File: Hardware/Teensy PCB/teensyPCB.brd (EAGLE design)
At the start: 100 x 50 mm, 27 parts, among them U2 USD-SOCKETNEW

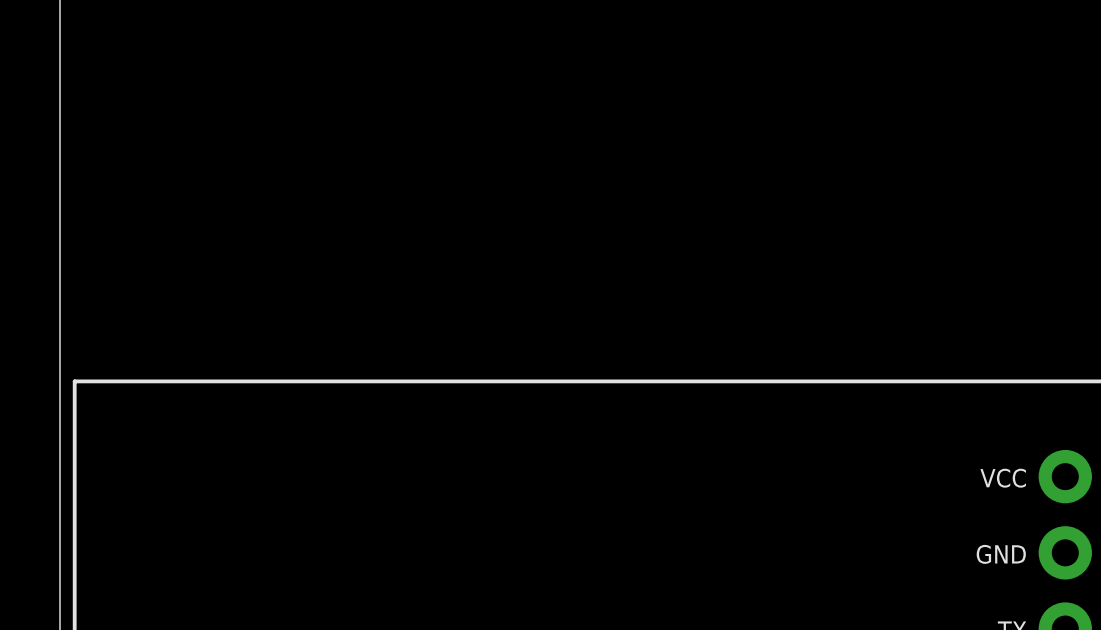
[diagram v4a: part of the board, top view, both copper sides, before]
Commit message: Added "state" push buttons
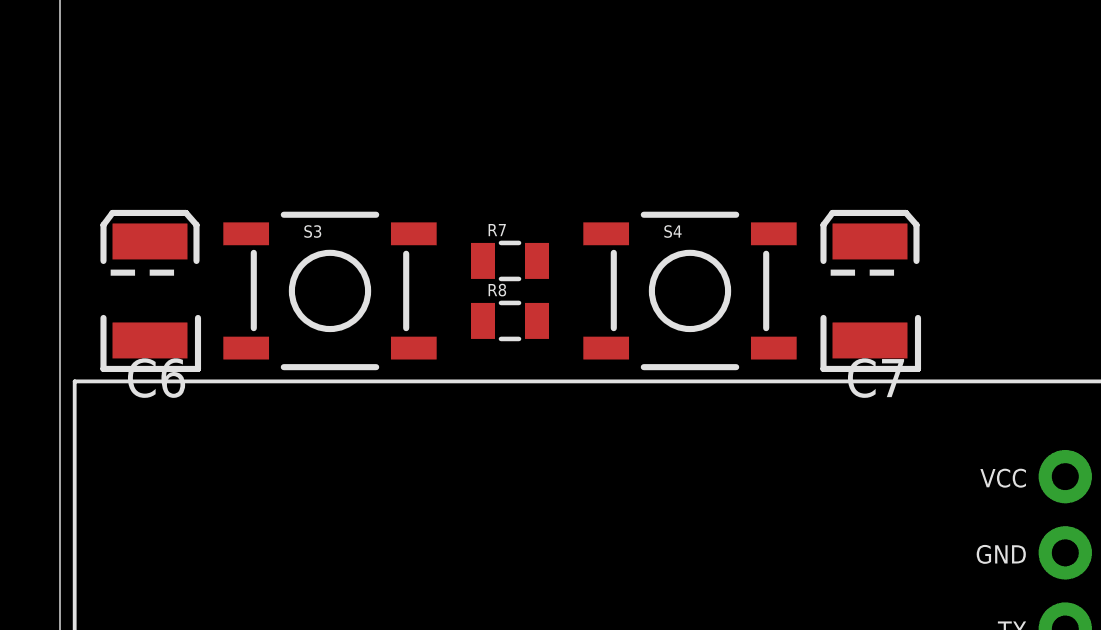
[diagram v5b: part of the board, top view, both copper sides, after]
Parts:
- added C6, C7: 100nF, SparkFun-Capacitors:EIA3528
- added R7, R8: 10k, SparkFun-Resistors:0805
- added S3, S4: TAC_SWITCHSMD, SparkFun-Retired:TACTILE-SWITCH-SMD
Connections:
- new net N$10: C7.C, R8.2, S4.3, S4.4, U$1.27
- new net N$4: C6.C, R7.2, S3.3, S3.4, U$1.28
- net 5V: now also C6.A, C7.A, S3.1, S3.2, S4.1, S4.2
- net GND: now also R7.1, R8.1
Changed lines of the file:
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@@
 <?xml version="1.0" encoding="utf-8"?>
 <!DOCTYPE eagle SYSTEM "eagle.dtd">
-<eagle version="7.5.0">
+<eagle version="7.2.0">
 <drawing>
 <settings>
@@
 <element name="C5" library="SparkFun-Capacitors" package="EIA3528" value="10uF" x="74" y="11"/>
 <element name="BAT1" library="SparkFun-Electromechanical" package="BATTCOM_20MM_PTH" value="" x="87" y="33" rot="R180"/>
+<element name="S3" library="SparkFun-Retired" package="TACTILE-SWITCH-SMD" value="TAC_SWITCHSMD" x="9" y="18">
+<attribute name="PROD_ID" value="SWCH-08247" x="9" y="32" size="1.778" layer="27" display="off"/>
+</element>
+<element name="R7" library="SparkFun-Resistors" package="0805" value="10k" x="15" y="19"/>
+<element name="C6" library="SparkFun-Capacitors" package="EIA3528" value="100nF" x="3" y="18" rot="R90"/>
+<element name="S4" library="SparkFun-Retired" package="TACTILE-SWITCH-SMD" value="TAC_SWITCHSMD" x="21" y="18">
+<attribute name="PROD_ID" value="SWCH-08247" x="9" y="32" size="1.778" layer="27" display="off"/>
+</element>
+<element name="R8" library="SparkFun-Resistors" package="0805" value="10k" x="15" y="17"/>
+<element name="C7" library="SparkFun-Capacitors" package="EIA3528" value="100nF" x="27" y="18" rot="R90"/>
 </elements>
 <signals>
@@
 <contactref element="R6" pad="1"/>
 <contactref element="BAT1" pad="2"/>
+<contactref element="R7" pad="1"/>
+<contactref element="R8" pad="1"/>
 <wire x1="95.15" y1="33" x2="79.92" y2="47.7" width="0" layer="19" extent="1-1"/>
 <wire x1="91" y1="15.1" x2="95.15" y2="33" width="0" layer="19" extent="1-1"/>
@@
 <wire x1="40.44" y1="7.1" x2="61.07" y2="3.246" width="0" layer="19" extent="1-1"/>
 <wire x1="9.92" y1="47.7" x2="30.8" y2="39.96" width="0" layer="19" extent="1-1"/>
+<wire x1="14.1" y1="19" x2="30.8" y2="39.96" width="0" layer="19" extent="1-1"/>
+<wire x1="14.1" y1="17" x2="14.1" y2="19" width="0" layer="19" extent="1-1"/>
 </signal>
 <signal name="3.3V">
@@
 <contactref element="U$4" pad="+5V"/>
 <contactref element="C1" pad="A"/>
+<contactref element="C6" pad="A"/>
+<contactref element="S3" pad="2"/>
+<contactref element="S3" pad="1"/>
+<contactref element="C7" pad="A"/>
+<contactref element="S4" pad="2"/>
+<contactref element="S4" pad="1"/>
 <wire x1="93.206" y1="14.095" x2="98.794" y2="14.095" width="0" layer="19" extent="1-1"/>
 <wire x1="88.225" y1="10.675" x2="93.206" y2="14.095" width="0" layer="19" extent="1-1"/>
@@
 <wire x1="66.15" y1="3.246" x2="64.9" y2="10" width="0" layer="19" extent="1-1"/>
 <wire x1="81.86" y1="2.13" x2="82.65" y2="11" width="0" layer="19" extent="1-1"/>
-<wire x1="37.53" y1="47.61" x2="64.9" y2="12" width="0" layer="19" extent="1-1"/>
-<wire x1="30.8" y1="47.58" x2="37.53" y2="47.61" width="0" layer="19" extent="1-1"/>
+<wire x1="27" y1="19.65" x2="64.9" y2="12" width="0" layer="19" extent="1-1"/>
+<wire x1="23.794" y1="19.905" x2="27" y2="19.65" width="0" layer="19" extent="1-1"/>
+<wire x1="18.206" y1="19.905" x2="23.794" y2="19.905" width="0" layer="19" extent="1-1"/>
+<wire x1="11.794" y1="19.905" x2="18.206" y2="19.905" width="0" layer="19" extent="1-1"/>
+<wire x1="6.206" y1="19.905" x2="11.794" y2="19.905" width="0" layer="19" extent="1-1"/>
+<wire x1="3" y1="19.65" x2="6.206" y2="19.905" width="0" layer="19" extent="1-1"/>
+<wire x1="30.8" y1="47.58" x2="27" y2="19.65" width="0" layer="19" extent="1-1"/>
+<wire x1="37.53" y1="47.61" x2="30.8" y2="47.58" width="0" layer="19" extent="1-1"/>
 </signal>
 <signal name="ARDUINO_RX">
@@
 <contactref element="U$1" pad="VUSB"/>
 </signal>
+<signal name="N$4">
+<contactref element="S3" pad="4"/>
+<contactref element="S3" pad="3"/>
+<contactref element="R7" pad="2"/>
+<contactref element="C6" pad="C"/>
+<contactref element="U$1" pad="28"/>
+<wire x1="15.9" y1="19" x2="61.8" y2="17.67" width="0" layer="19" extent="1-1"/>
+<wire x1="11.794" y1="16.095" x2="15.9" y2="19" width="0" layer="19" extent="1-1"/>
+<wire x1="6.206" y1="16.095" x2="11.794" y2="16.095" width="0" layer="19" extent="1-1"/>
+<wire x1="3" y1="16.35" x2="6.206" y2="16.095" width="0" layer="19" extent="1-1"/>
+</signal>
+<signal name="N$10">
+<contactref element="S4" pad="4"/>
+<contactref element="S4" pad="3"/>
+<contactref element="R8" pad="2"/>
+<contactref element="C7" pad="C"/>
+<contactref element="U$1" pad="27"/>
+<wire x1="27" y1="16.35" x2="61.8" y2="20.21" width="0" layer="19" extent="1-1"/>
+<wire x1="23.794" y1="16.095" x2="27" y2="16.35" width="0" layer="19" extent="1-1"/>
+<wire x1="18.206" y1="16.095" x2="23.794" y2="16.095" width="0" layer="19" extent="1-1"/>
+<wire x1="15.9" y1="17" x2="18.206" y2="16.095" width="0" layer="19" extent="1-1"/>
+</signal>
 </signals>

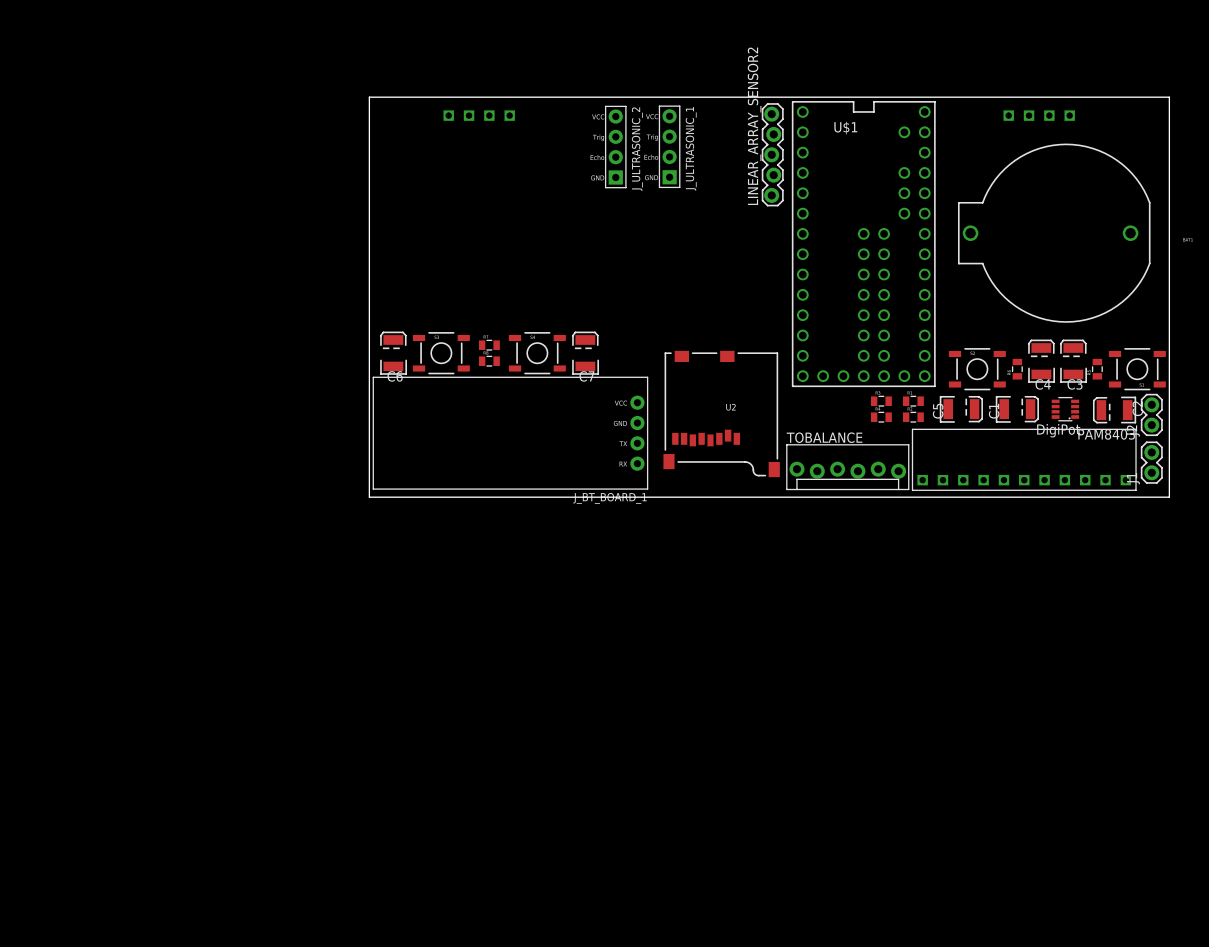
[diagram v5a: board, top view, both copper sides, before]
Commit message: Updated hole spacing and layout
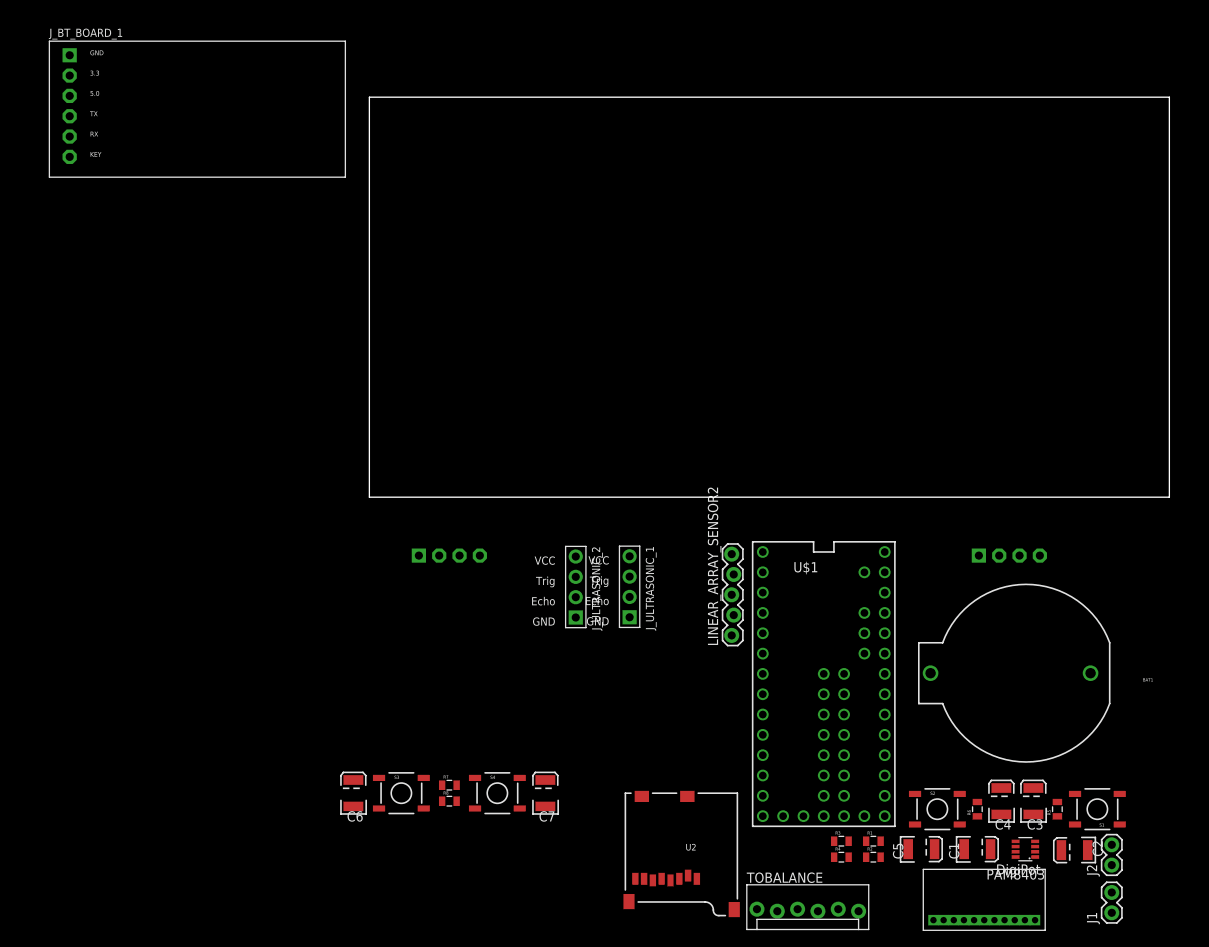
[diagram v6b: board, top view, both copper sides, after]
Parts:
- moved J_BT_BOARD_1 65.4 mm to (-40.0, 40.0), turned to 0 degrees
- moved BAT1 55.2 mm to (82.0, -22.0)
- moved C1 55.2 mm to (76.0, -44.0)
- moved C2 55.2 mm to (88.2, -44.1)
- moved C3 55.2 mm to (83.0, -38.0)
- moved C4 55.2 mm to (79.0, -38.0)
- moved C5 55.2 mm to (69.0, -44.0)
- moved C6 55.2 mm to (-2.00, -37.0)
- moved C7 55.2 mm to (22.0, -37.0)
- moved J1 55.2 mm to (92.8, -52.0)
- moved J2 55.2 mm to (92.8, -46.0)
- moved J_ULTRASONIC_1 55.2 mm to (32.5, -11.2)
- moved J_ULTRASONIC_2 55.2 mm to (25.8, -11.2)
- moved LINEAR_ARRAY_SENSOR2 55.2 mm to (45.4, -17.3)
- moved R1 55.2 mm to (63.0, -43.0)
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
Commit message: layout work
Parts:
- removed R1, R2, R3, R4: 4.7k, SparkFun-Resistors:0805
- C3, C4, C6, C7: value 100nF -> 1.0uF; device SparkFun-Capacitors:EIA3528 -> SparkFun-Capacitors:0805
- S1: value TAC_SWITCHSMD -> UP
- S2: value TAC_SWITCHSMD -> DOWN
- S3: value TAC_SWITCHSMD -> LEFT
- S4: value TAC_SWITCHSMD -> RIGHT
- U$4: value AUDIOAMP -> AUDIOAMPEBAY_VERSION
- moved C3 93.7 mm to (2.50, 10.0), flipped to the bottom, turned to 270 degrees
- moved S1 93.2 mm to (15.0, 15.0), flipped to the bottom, turned to 0 degrees
- moved U$4 91.6 mm to (73.8, 41.2), turned to 270 degrees
- moved R5 89.2 mm to (15.0, 15.0), turned to 180 degrees
- moved BAT1 88.1 mm to (13.8, 33.8), turned to 0 degrees
- moved C4 78.0 mm to (17.5, 10.0), flipped to the bottom, turned to 270 degrees
- moved R6 75.2 mm to (15.0, 5.00), turned to 0 degrees
- moved J_BT_BOARD_1 72.9 mm to (32.5, 47.5), flipped to the bottom, turned to 180 degrees
- moved S2 71.2 mm to (15.0, 5.00), flipped to the bottom
- moved J_ULTRASONIC_2 67.3 mm to (66.2, 42.5)
- moved J1 67.0 mm to (92.5, 15.0)
- moved J2 61.2 mm to (97.5, 15.0)
- moved TOBALANCE 56.7 mm to (43.8, 5.00)
- moved U$1 56.3 mm to (50.0, 32.5)
- moved U$2 55.2 mm to (85.0, 35.0)
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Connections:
- net 5V: now also C3.1, C4.1, C6.1, C7.1; no longer C3.A, C4.A, C6.A, C7.A, R1.2, R2.2, R3.2, R4.2
- net GND: now also U$4.AGND, U$4.GND; no longer U$4.GND0, U$4.GND1, U$4.GND2
- net N$10: now also C4.2; no longer C7.C
- net N$2: now also C7.2; no longer C4.C
- net N$4: now also C3.2; no longer C6.C
- net N$9: now also C6.2; no longer C3.C
- net SCL0: no longer R2.1
- net SCL1: no longer R4.1
- net SDA0: no longer R1.1
- net SDA1: no longer R3.1
- net SW: no longer U$4.SW

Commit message: more layout
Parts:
- removed J_ULTRASONIC_1, J_ULTRASONIC_2: HC-SR04, HC-SR04:HC-SR04_FOOTPRINT
- removed LINEAR_ARRAY_SENSOR2: (no value), SparkFun-Connectors:1X05_LOCK
- added C8: 10uF, SparkFun-Capacitors:0805
- added C9: 1uF, SparkFun-Capacitors:0805
- added LIN_ARRAY: (no value), SparkFun-Connectors:1X05_LOCK
- added USONIC1, USONIC2: HC-SR04, HC-SR04:HC-SR04_FOOTPRINT
- C2: device SparkFun-Capacitors:EIA3528 -> SparkFun-Capacitors:0805
- C5: value 10uF -> 47uF
- moved U2 46.9 mm to (71.9, 16.2)
- moved J_BT_BOARD_1 46.2 mm to (40.0, 1.88), turned to 0 degrees
- moved TOBALANCE 31.1 mm to (35.6, 35.0), turned to 90 degrees
- moved C2 26.8 mm to (65.6, 23.8)
- moved C1 24.3 mm to (71.2, 25.6), turned to 90 degrees
- moved U$5 19.3 mm to (63.8, 20.0), turned to 180 degrees
- moved C5 7.59 mm to (67.5, 5.00)
- moved J1 0.62 mm to (91.9, 15.0)
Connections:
- net 3.3V: now also C5.A, C9.1, LIN_ARRAY.4; no longer LINEAR_ARRAY_SENSOR2.4
- net 5V: now also USONIC1.VCC, USONIC2.VCC; no longer J_ULTRASONIC_1.VCC, J_ULTRASONIC_2.VCC
- net AOUT: now also LIN_ARRAY.1; no longer LINEAR_ARRAY_SENSOR2.1
- net CLK: now also LIN_ARRAY.3; no longer LINEAR_ARRAY_SENSOR2.3
- net DAC: now also C8.2; no longer C5.A
- net ECHO: now also USONIC2.ECHO; no longer J_ULTRASONIC_1.ECHO
- net ECHO2: now also USONIC1.ECHO; no longer J_ULTRASONIC_2.ECHO
- net GND: now also C5.C, C9.2, LIN_ARRAY.5, USONIC1.GND, USONIC2.GND; no longer J_ULTRASONIC_1.GND, J_ULTRASONIC_2.GND, LINEAR_ARRAY_SENSOR2.5
- net N$1: now also C2.1; no longer C2.C
- net N$3: now also C8.1; no longer C5.C
- net SI: now also LIN_ARRAY.2; no longer LINEAR_ARRAY_SENSOR2.2
- net TRIG: now also USONIC2.TRIG; no longer J_ULTRASONIC_1.TRIG
- net TRIG2: now also USONIC1.TRIG; no longer J_ULTRASONIC_2.TRIG
- net WOUT: now also C2.2; no longer C2.A
